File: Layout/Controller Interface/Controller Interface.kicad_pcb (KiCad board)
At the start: 2 copper layers, 50 x 50 mm, 71 parts, among them J1 USB_C_Receptacle_USB2.0, J2 Controller 2, J3 Controller 3, J4 Controller 4, J6 Conn_01x02_Pin, J7 Controller 1, Q1 AO3401A, Q2 AO3401A, Q3 AO3401A, SW1 PWR, SW3 SW_PAIR, SW4 SW_BOOT, U1 W25Q32JVSS, U2 RP2040, U4 MCP73812T-420I-OT, U5 TPS613223ADBV, U7 MIC5504-3.3YM5, Y2 Crystal_GND24

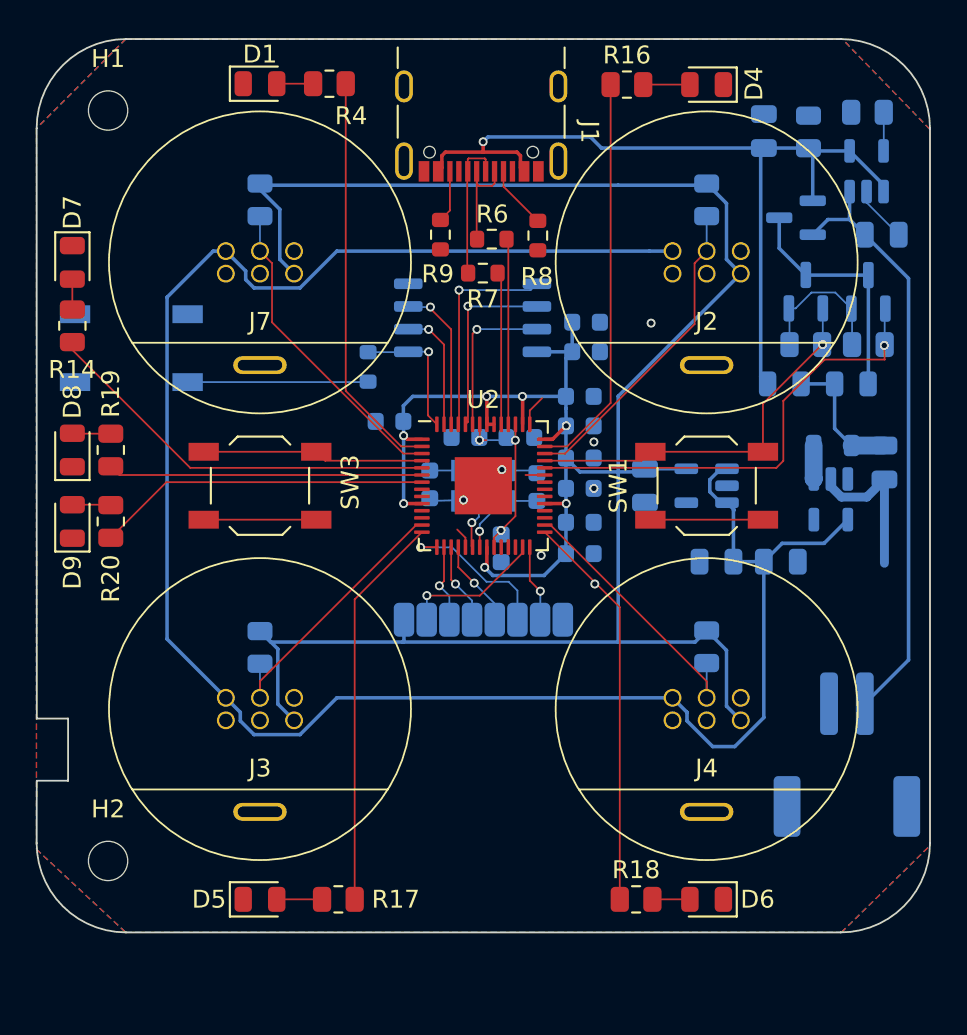
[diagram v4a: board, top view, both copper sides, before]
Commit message: Create a separate board for the LEDs
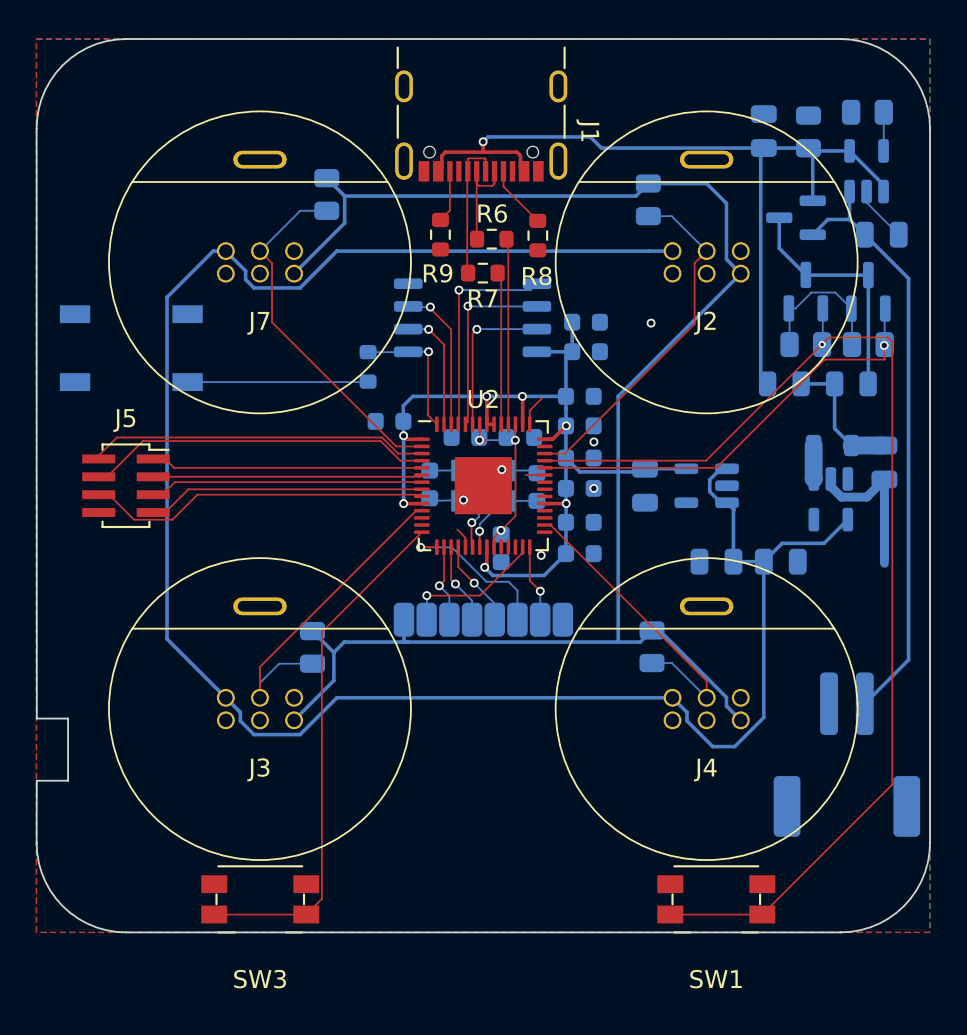
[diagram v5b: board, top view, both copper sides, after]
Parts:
- removed D1, D4, D5, D6, D7, D8, D9: LED, LED_SMD:LED_0805_2012Metric
- removed H1, H2: MountingHole_Pad, MountingHole:MountingHole_2.2mm_M2_DIN965
- removed R14, R16, R17, R18, R19, R20, R4: 100, Resistor_SMD:R_0805_2012Metric
- added J5: Conn_01x08_Socket, Connector_PinSocket_1.00mm:PinSocket_2x04_P1.00mm_Vertical_SMD, F.Cu at (135.8, 94.9)
- SW1, SW3: footprint Button_Switch_SMD:SW_SPST_TL3342 -> Button_Switch_SMD:Panasonic_EVQPUK_EVQPUB
- moved SW1 23.2 mm to (168.8, 118.0), turned to 180 degrees
- moved SW3 23.2 mm to (143.3, 118.0), turned to 180 degrees
- moved R15 3.75 mm to (147.0, 78.6)
- moved R1 3.26 mm to (165.0, 78.9)
- moved R3 3.06 mm to (165.2, 103.9)
- moved R2 2.94 mm to (146.2, 104.0)
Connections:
- U2 pad 11: unconnected-(U2-GPIO8-Pad11) -> DATA_3
- U2 pad 13: DATA_3 -> unconnected-(U2-GPIO10-Pad13)
- U2 pad 14: CONT_3 -> /Processor/PAIR
- U2 pad 2: CONT_1 -> DATA_1
- U2 pad 29: CONT_4 -> unconnected-(U2-GPIO18-Pad29)
- U2 pad 3: DATA_1 -> TX_LED
- U2 pad 4: /Processor/PAIR -> /Processor/PWR_LED
- U2 pad 41: CONT_2 -> unconnected-(U2-GPIO29_ADC3-Pad41)
- U2 pad 5: /Processor/PWR_LED -> CONT_1
- U2 pad 6: TX_LED -> CONT_2
- U2 pad 7: RX_LED -> CONT_3
- U2 pad 8: unconnected-(U2-GPIO6-Pad8) -> CONT_4
- U2 pad 9: unconnected-(U2-GPIO7-Pad9) -> RX_LED
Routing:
- net PWR_SW: track 21.8 -> 64.7 mm
- net /Processor/PAIR: track 12.4 -> 29.2 mm
- net GND: track 32.6 -> 20.0 mm
- net +3.3V: track 150.9 -> 143.3 mm
- net CONT_1: track 22.7 -> 15.2 mm
- net CONT_2: track 22.5 -> 15.1 mm
- net CONT_3: track 22.1 -> 15.3 mm
- net CONT_4: track 22.3 -> 15.6 mm, vias 1 -> 0
- net /Processor/PWR_LED: track 22.7 -> 19.4 mm
- net DATA_3: track 15.5 -> 18.6 mm
- net Net-(D4-A): track 2.61 -> 0.00 mm
- net DATA_1: track 17.7 -> 20.2 mm
- net Net-(D5-A): track 2.54 -> 0.00 mm
- net Net-(D9-A): track 2.16 -> 0.00 mm
- net Net-(D8-A): track 2.16 -> 0.00 mm
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
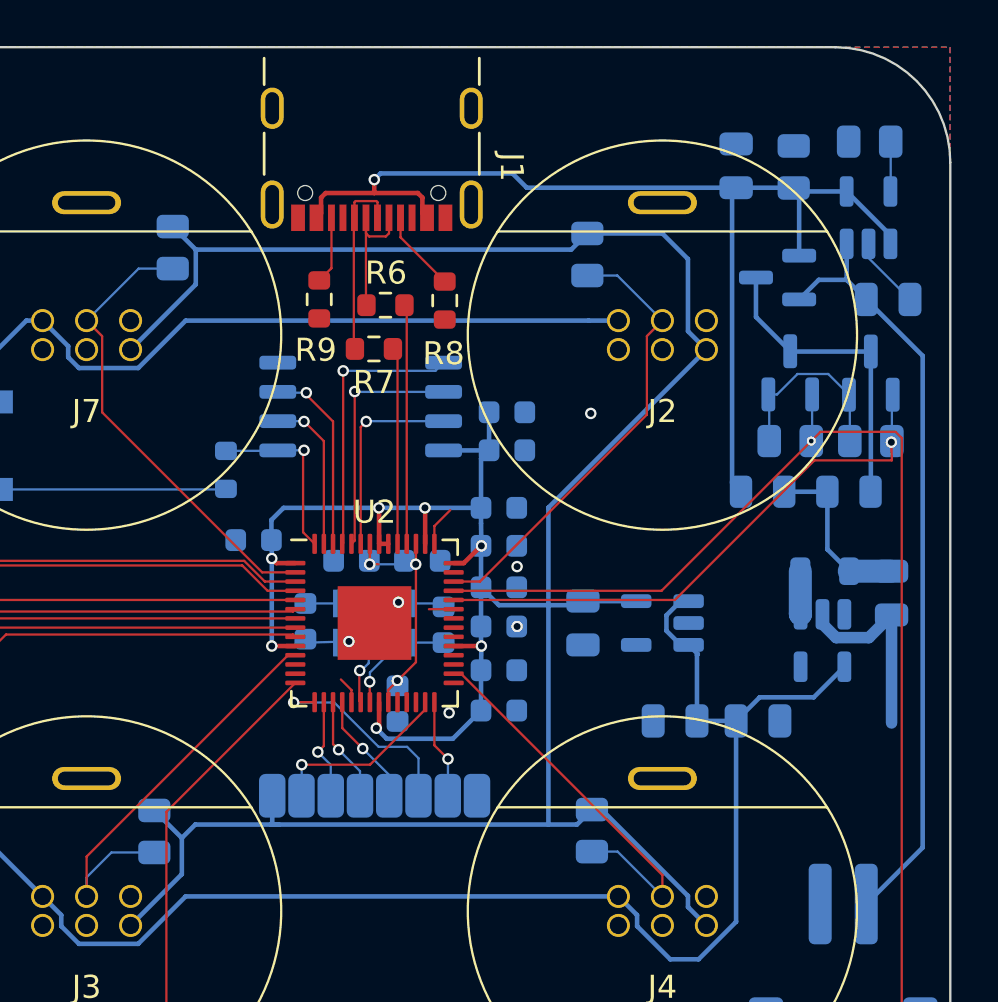
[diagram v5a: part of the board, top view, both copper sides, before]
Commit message: Use separate board for lights
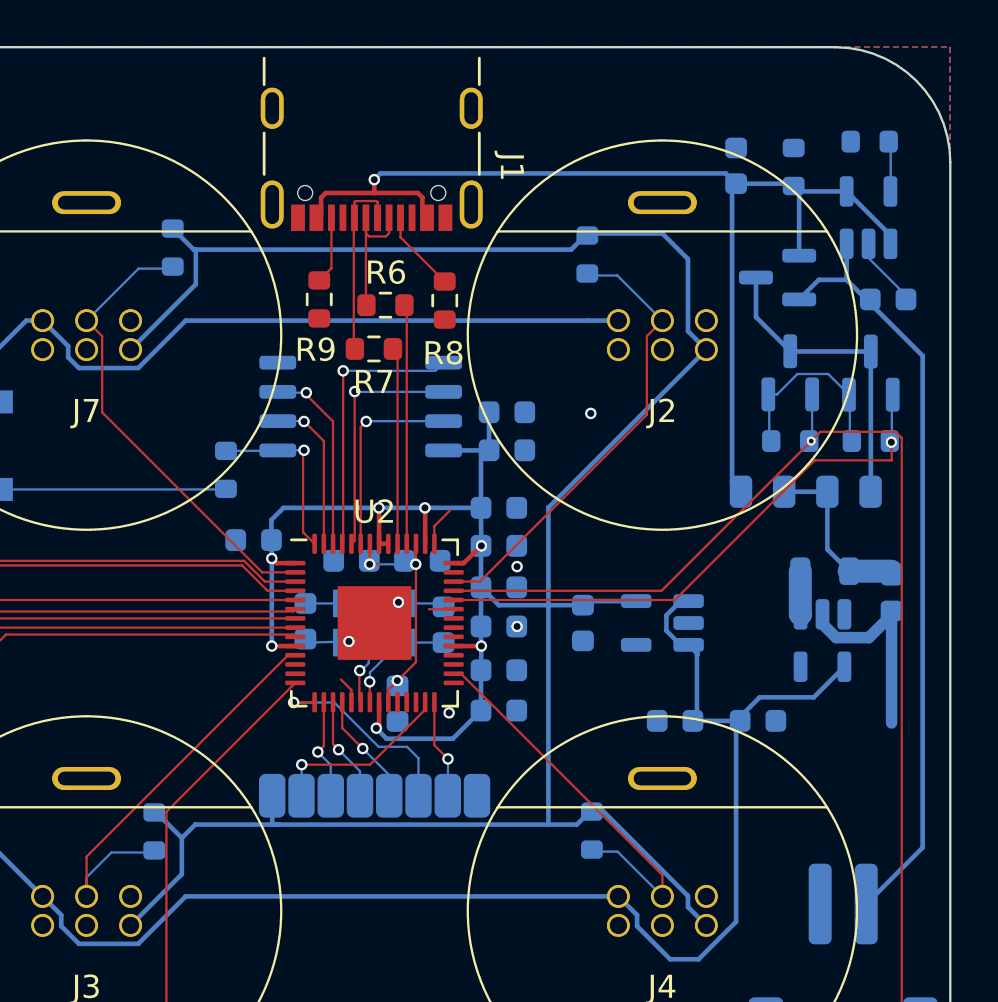
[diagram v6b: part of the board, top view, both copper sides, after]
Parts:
- C10, C5, C6, C7, C8, C9: footprint Capacitor_SMD:C_0805_2012Metric -> Capacitor_SMD:C_0603_1608Metric
- R1, R10, R11, R12, R15, R2, R3, R5: footprint Resistor_SMD:R_0805_2012Metric -> Resistor_SMD:R_0603_1608Metric
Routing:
- net +3.3V: track 143.3 -> 142.7 mm
